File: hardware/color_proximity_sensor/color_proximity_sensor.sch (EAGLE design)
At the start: 69 parts, among them IC1 TCS37725FN, IC2 APDS-9800-021, IC4 LM25011MY, IC5 ATXMEGA64DA-AU, J1 PDI_ATMEL_WIDTH, Q1 16 MHz, T1 BC847CDXV6T1G, T4 BC847CDXV6T1G

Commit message: few changes on board
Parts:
- C33: value 10µF 25V -> 22UF-C_10V; device robotter_capacitor:10UF-C_25V -> robotter_capacitor:22UF-C_10V
- R20, R25: value 10K-F -> 3K09-F; device robotter_resistor:10K-F -> robotter_resistor:3K09-F
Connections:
- net GND: now also IC4.THERMAL_GND
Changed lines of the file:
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@@
 <part name="C31" library="robotter_capacitor" deviceset="10NF" device="-F" value="10nF 50V"/>
 <part name="C32" library="robotter_capacitor" deviceset="100NF" device="-F" value="100nF 50V"/>
-<part name="C33" library="robotter_capacitor" deviceset="10UF" device="-C_25V" value="10µF 25V"/>
+<part name="C33" library="robotter_capacitor" deviceset="22UF" device="-C_10V" value="22UF-C_10V"/>
 <part name="D8" library="robotter_diode" deviceset="B160-13F" device="" value="B160-13F"/>
 <part name="L1" library="robotter_inductor" deviceset="SDR0805" device="-270KL"/>
@@
 <part name="C16" library="robotter_capacitor" deviceset="100NF" device="-F" value="100nF 50V"/>
 <part name="R19" library="robotter_resistor" deviceset="10K" device="-F"/>
-<part name="R20" library="robotter_resistor" deviceset="10K" device="-F"/>
+<part name="R20" library="robotter_resistor" deviceset="3K09" device="-F"/>
 <part name="R21" library="robotter_resistor" deviceset="10K" device="-F"/>
 <part name="R23" library="robotter_resistor" deviceset="10K" device="-F"/>
-<part name="R25" library="robotter_resistor" deviceset="10K" device="-F"/>
+<part name="R25" library="robotter_resistor" deviceset="3K09" device="-F"/>
 <part name="L2" library="robotter_inductor" deviceset="FERRITE_220OHMS" device="" value="220 ohms"/>
 <part name="C17" library="robotter_capacitor" deviceset="100NF" device="-F" value="100nF 50V"/>
@@
 <instance part="+3V17" gate="G$1" x="508" y="144.78"/>
 <instance part="GND23" gate="1" x="347.98" y="106.68"/>
-<instance part="IC4" gate="G$1" x="444.5" y="132.08"/>
+<instance part="IC4" gate="G$1" x="444.5" y="134.62"/>
 <instance part="C22" gate="G$1" x="396.24" y="132.08"/>
 <instance part="C30" gate="G$1" x="408.94" y="139.7"/>
@@
 <instance part="R60" gate="G$1" x="487.68" y="116.84" rot="R270"/>
 <instance part="R61" gate="G$1" x="487.68" y="132.08" rot="R270"/>
-<instance part="GND24" gate="1" x="444.5" y="106.68"/>
+<instance part="GND24" gate="1" x="447.04" y="106.68"/>
 <instance part="GND25" gate="1" x="462.28" y="124.46"/>
 <instance part="R13" gate="G$1" x="358.14" y="132.08" rot="R90"/>
@@
 <wire x1="408.94" y1="109.22" x2="426.72" y2="109.22" width="0.1524" layer="91"/>
 <wire x1="426.72" y1="109.22" x2="444.5" y2="109.22" width="0.1524" layer="91"/>
-<wire x1="444.5" y1="109.22" x2="444.5" y2="116.84" width="0.1524" layer="91"/>
+<wire x1="444.5" y1="109.22" x2="447.04" y2="109.22" width="0.1524" layer="91"/>
+<wire x1="447.04" y1="109.22" x2="447.04" y2="116.84" width="0.1524" layer="91"/>
 <pinref part="C31" gate="G$1" pin="2"/>
 <wire x1="426.72" y1="114.3" x2="426.72" y2="109.22" width="0.1524" layer="91"/>
-<wire x1="444.5" y1="109.22" x2="487.68" y2="109.22" width="0.1524" layer="91"/>
+<wire x1="447.04" y1="109.22" x2="487.68" y2="109.22" width="0.1524" layer="91"/>
 <pinref part="R60" gate="G$1" pin="2"/>
 <wire x1="487.68" y1="109.22" x2="487.68" y2="111.76" width="0.1524" layer="91"/>
 <junction x="426.72" y="109.22"/>
-<junction x="444.5" y="109.22"/>
+<junction x="447.04" y="109.22"/>
 <pinref part="C30" gate="G$1" pin="2"/>
 <wire x1="408.94" y1="134.62" x2="408.94" y2="109.22" width="0.1524" layer="91"/>
@@
 <junction x="487.68" y="109.22"/>
 <junction x="408.94" y="109.22"/>
+<pinref part="IC4" gate="G$1" pin="THERMAL_GND"/>
+<wire x1="444.5" y1="116.84" x2="444.5" y2="109.22" width="0.1524" layer="91"/>
+<junction x="444.5" y="109.22"/>
 </segment>
 <segment>
 <pinref part="IC4" gate="G$1" pin="CSG"/>
-<wire x1="454.66" y1="129.54" x2="454.66" y2="127" width="0.1524" layer="91"/>
 <pinref part="R22" gate="G$1" pin="1"/>
-<wire x1="454.66" y1="127" x2="462.28" y2="127" width="0.1524" layer="91"/>
+<wire x1="457.2" y1="129.54" x2="457.2" y2="127" width="0.1524" layer="91"/>
+<wire x1="457.2" y1="127" x2="462.28" y2="127" width="0.1524" layer="91"/>
 <pinref part="GND25" gate="1" pin="GND"/>
 <junction x="462.28" y="127"/>
@@
 </segment>
 <segment>
-<wire x1="53.34" y1="68.58" x2="53.34" y2="33.02" width="0.1524" layer="91"/>
-<wire x1="53.34" y1="33.02" x2="73.66" y2="33.02" width="0.1524" layer="91"/>
-<wire x1="73.66" y1="33.02" x2="86.36" y2="33.02" width="0.1524" layer="91"/>
-<wire x1="86.36" y1="33.02" x2="101.6" y2="33.02" width="0.1524" layer="91"/>
+<wire x1="73.66" y1="33.02" x2="101.6" y2="33.02" width="0.1524" layer="91"/>
 <wire x1="101.6" y1="33.02" x2="109.22" y2="33.02" width="0.1524" layer="91"/>
 <wire x1="109.22" y1="33.02" x2="144.78" y2="33.02" width="0.1524" layer="91"/>
 <wire x1="144.78" y1="33.02" x2="144.78" y2="38.1" width="0.1524" layer="91"/>
 <wire x1="109.22" y1="53.34" x2="109.22" y2="33.02" width="0.1524" layer="91"/>
-<wire x1="86.36" y1="48.26" x2="86.36" y2="33.02" width="0.1524" layer="91"/>
 <wire x1="73.66" y1="73.66" x2="73.66" y2="33.02" width="0.1524" layer="91"/>
 <pinref part="GND9" gate="1" pin="GND"/>
 <junction x="101.6" y="33.02"/>
-<junction x="73.66" y="33.02"/>
-<junction x="86.36" y="33.02"/>
 <junction x="109.22" y="33.02"/>
 <pinref part="T4" gate="-Q1" pin="E"/>
@@
 <pinref part="IC4" gate="G$1" pin="SW"/>
 <pinref part="D8" gate="G$1" pin="C"/>
-<wire x1="462.28" y1="142.24" x2="454.66" y2="142.24" width="0.1524" layer="91"/>
+<wire x1="462.28" y1="142.24" x2="457.2" y2="142.24" width="0.1524" layer="91"/>
 <pinref part="C32" gate="G$1" pin="2"/>
 <junction x="462.28" y="142.24"/>
@@
 <pinref part="IC4" gate="G$1" pin="CS"/>
 <pinref part="D8" gate="G$1" pin="A"/>
-<wire x1="462.28" y1="137.16" x2="454.66" y2="137.16" width="0.1524" layer="91"/>
+<wire x1="462.28" y1="137.16" x2="457.2" y2="137.16" width="0.1524" layer="91"/>
 <pinref part="R22" gate="G$1" pin="2"/>
 <junction x="462.28" y="137.16"/>
@@
 <pinref part="IC4" gate="G$1" pin="FB"/>
 <pinref part="R60" gate="G$1" pin="1"/>
-<wire x1="454.66" y1="121.92" x2="487.68" y2="121.92" width="0.1524" layer="91"/>
+<wire x1="457.2" y1="121.92" x2="487.68" y2="121.92" width="0.1524" layer="91"/>
 <pinref part="R61" gate="G$1" pin="2"/>
 <wire x1="487.68" y1="127" x2="487.68" y2="121.92" width="0.1524" layer="91"/>
@@
 <segment>
 <pinref part="IC4" gate="G$1" pin="BST"/>
-<wire x1="454.66" y1="147.32" x2="457.2" y2="147.32" width="0.1524" layer="91"/>
 <wire x1="457.2" y1="147.32" x2="457.2" y2="149.86" width="0.1524" layer="91"/>
 <pinref part="C32" gate="G$1" pin="1"/>

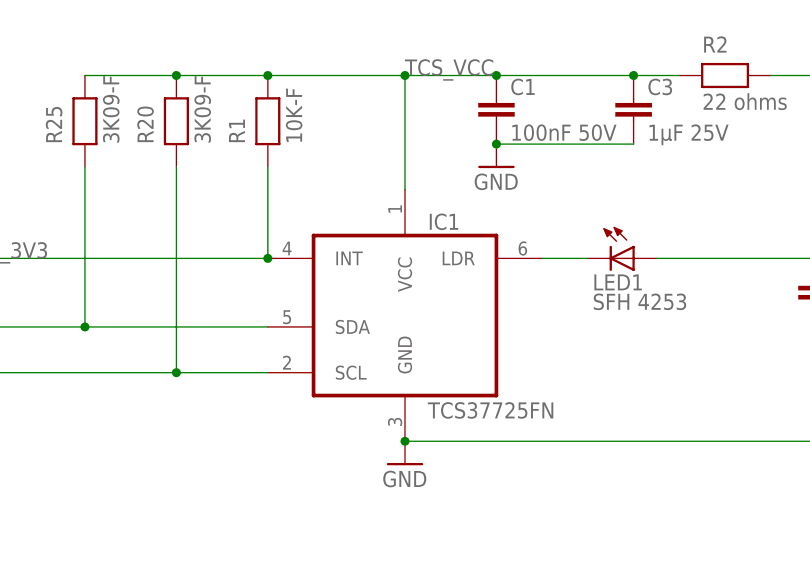
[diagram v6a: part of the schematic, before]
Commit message: corrected tcs37725 and b160, need rerouting tcs37725
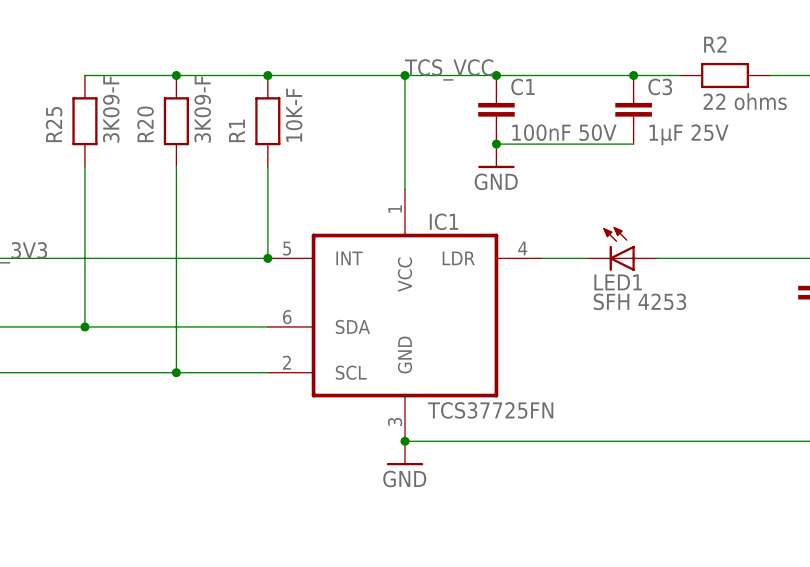
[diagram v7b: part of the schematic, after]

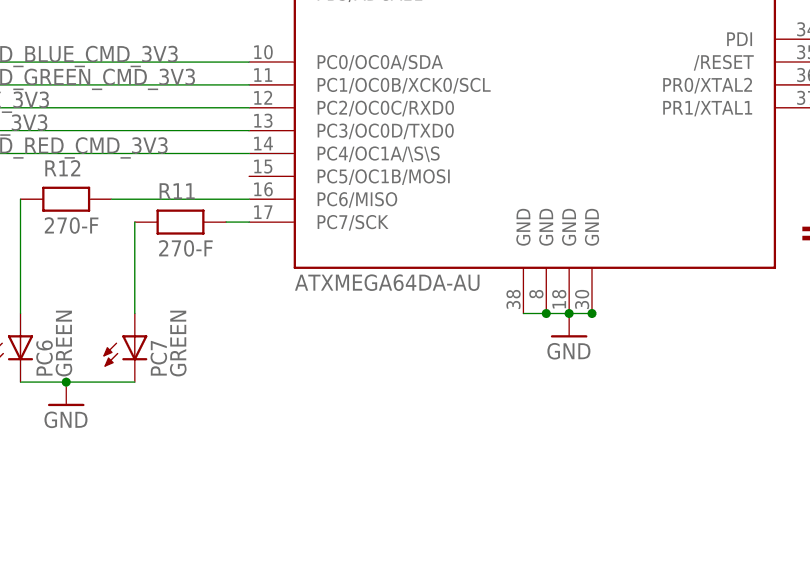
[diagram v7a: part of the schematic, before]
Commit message: v2 rerouted and ic5 (atxmega) value modified
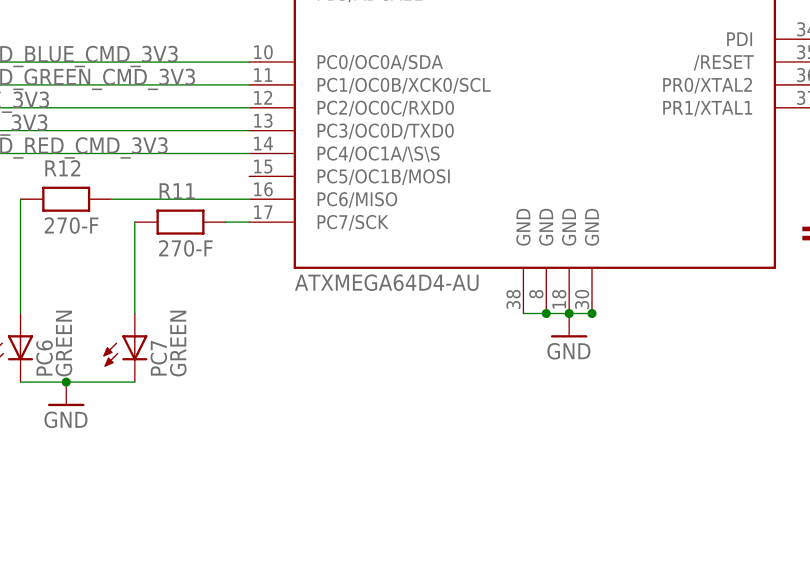
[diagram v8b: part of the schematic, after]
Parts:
- IC5: value ATXMEGA64DA-AU -> ATXMEGA64D4-AU
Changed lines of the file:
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@@
 <part name="R17" library="robotter_resistor" deviceset="1K" device="-A" value="1k 1W"/>
 <part name="R18" library="robotter_resistor" deviceset="1K" device="-A" value="1k 1W"/>
-<part name="IC5" library="robotter_ic" deviceset="ATXMEGA64D4" device="-AU" value="ATXMEGA64DA-AU"/>
+<part name="IC5" library="robotter_ic" deviceset="ATXMEGA64D4" device="-AU" value="ATXMEGA64D4-AU"/>
 <part name="+3V3" library="supply1" deviceset="+3V3" device=""/>
 <part name="+3V4" library="supply1" deviceset="+3V3" device=""/>
